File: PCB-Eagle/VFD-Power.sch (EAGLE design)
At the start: 24 parts, among them IC1 74HC132D, IC3 ZXBM5210

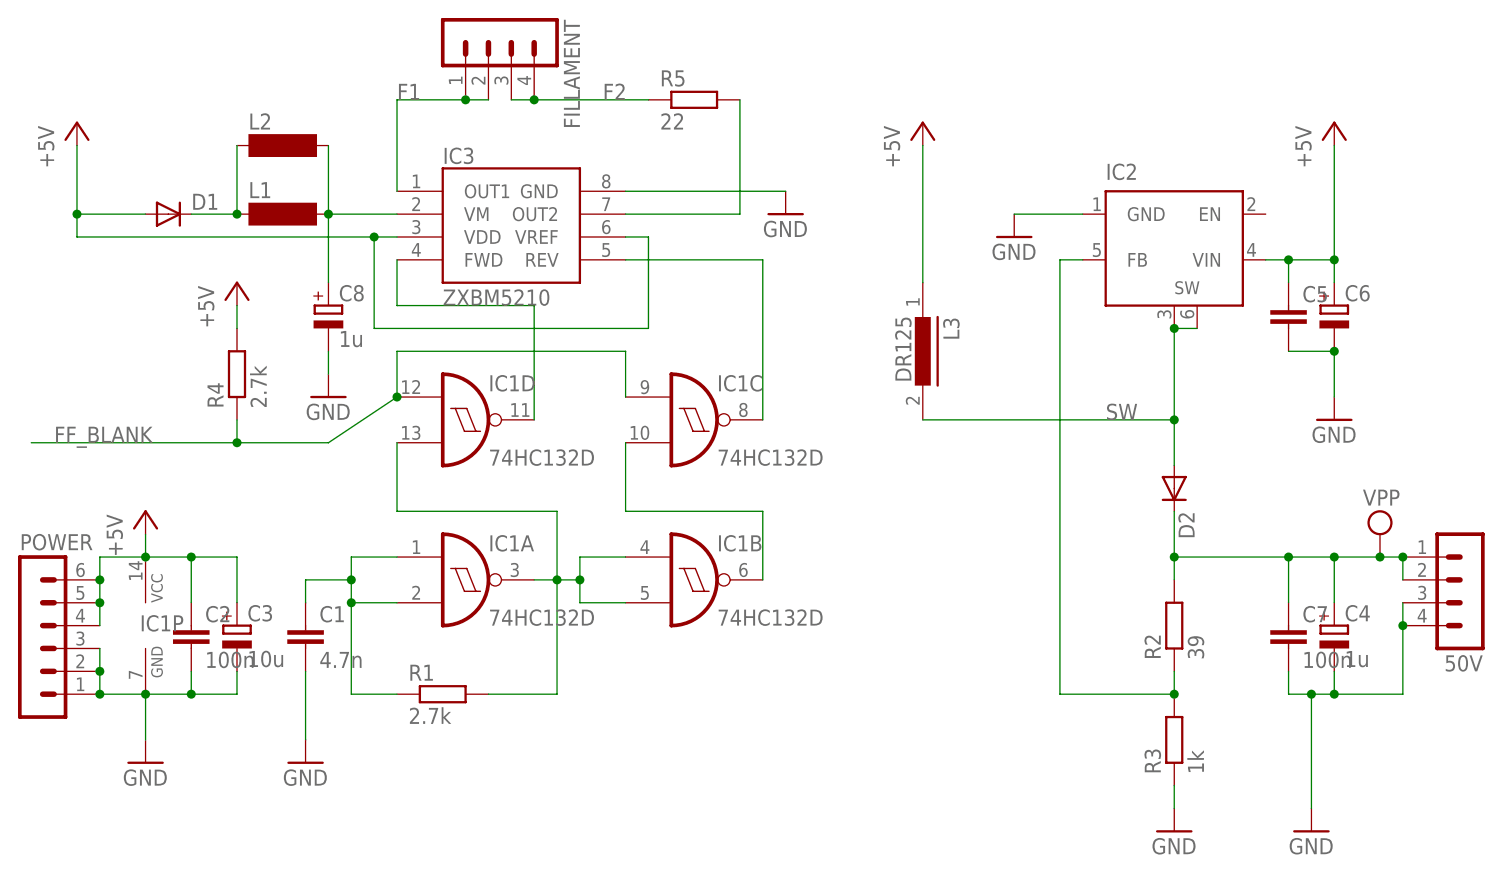
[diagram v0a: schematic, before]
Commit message: fixed Up Converter R9/R10 twist, adjusted values for 50V
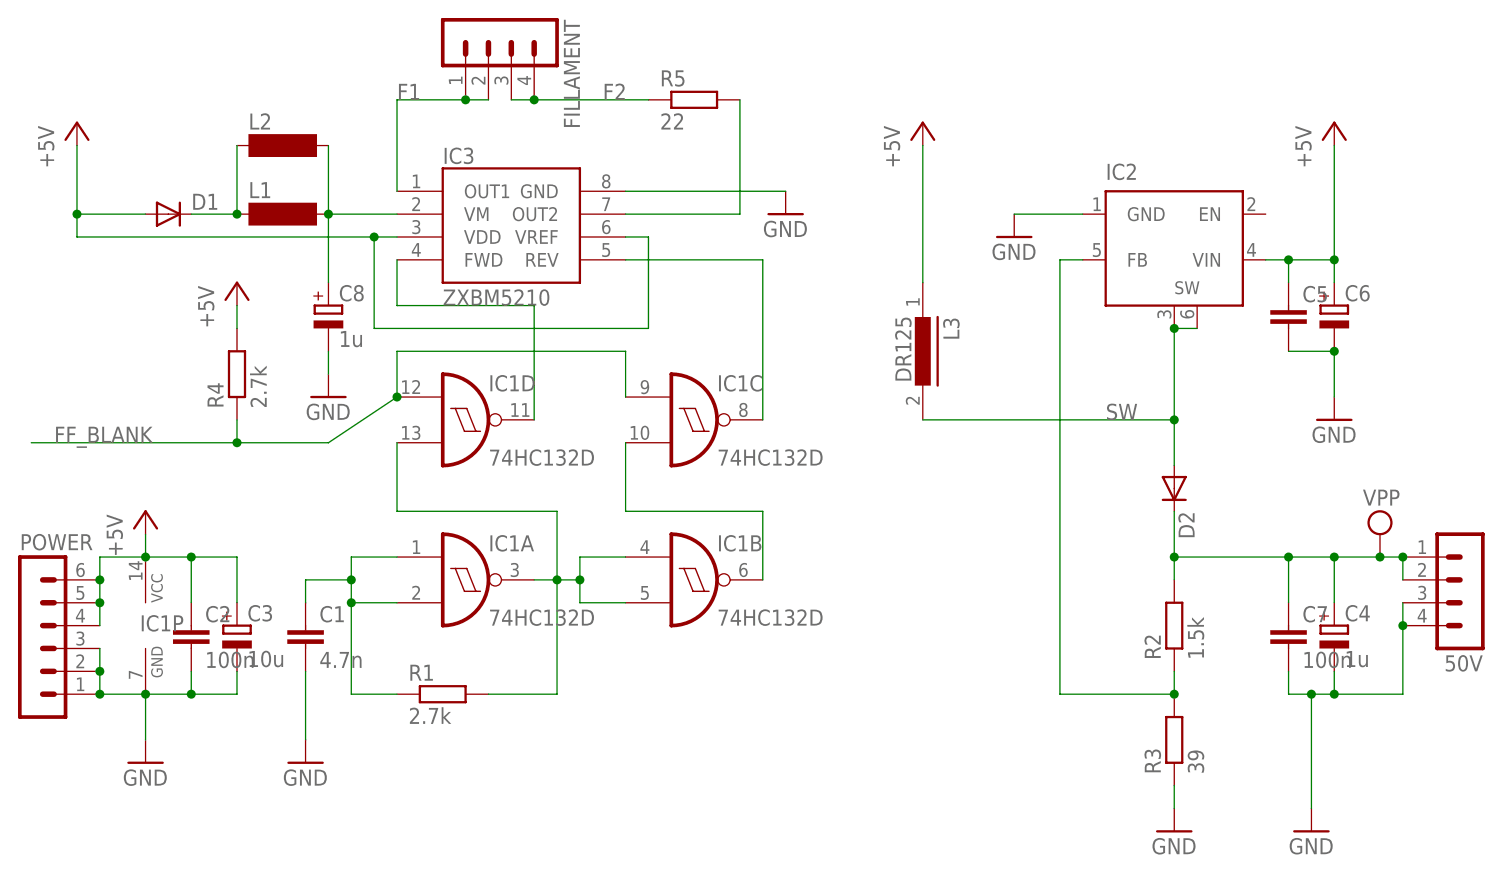
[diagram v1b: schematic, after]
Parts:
- R2: value 39 -> 1.5k
- R3: value 1k -> 39
